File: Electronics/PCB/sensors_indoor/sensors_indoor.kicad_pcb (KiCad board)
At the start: 4 copper layers, 50 x 50 mm, 21 parts, among them J1 USB4125-GF-A, J2 Conn_ST_STDC14, J3 B5B-ZR, U1 STM32WBA5MMG, U10 MIC5219-3.3YM5, U2 SHT45-AD1F, U3 SCD41-D-R2, U4 SGP41, U5 LPS22DF, U6 TSOP38436, U7 FM24CL16B, U8 SPS30, U9 OPT4001DTSR

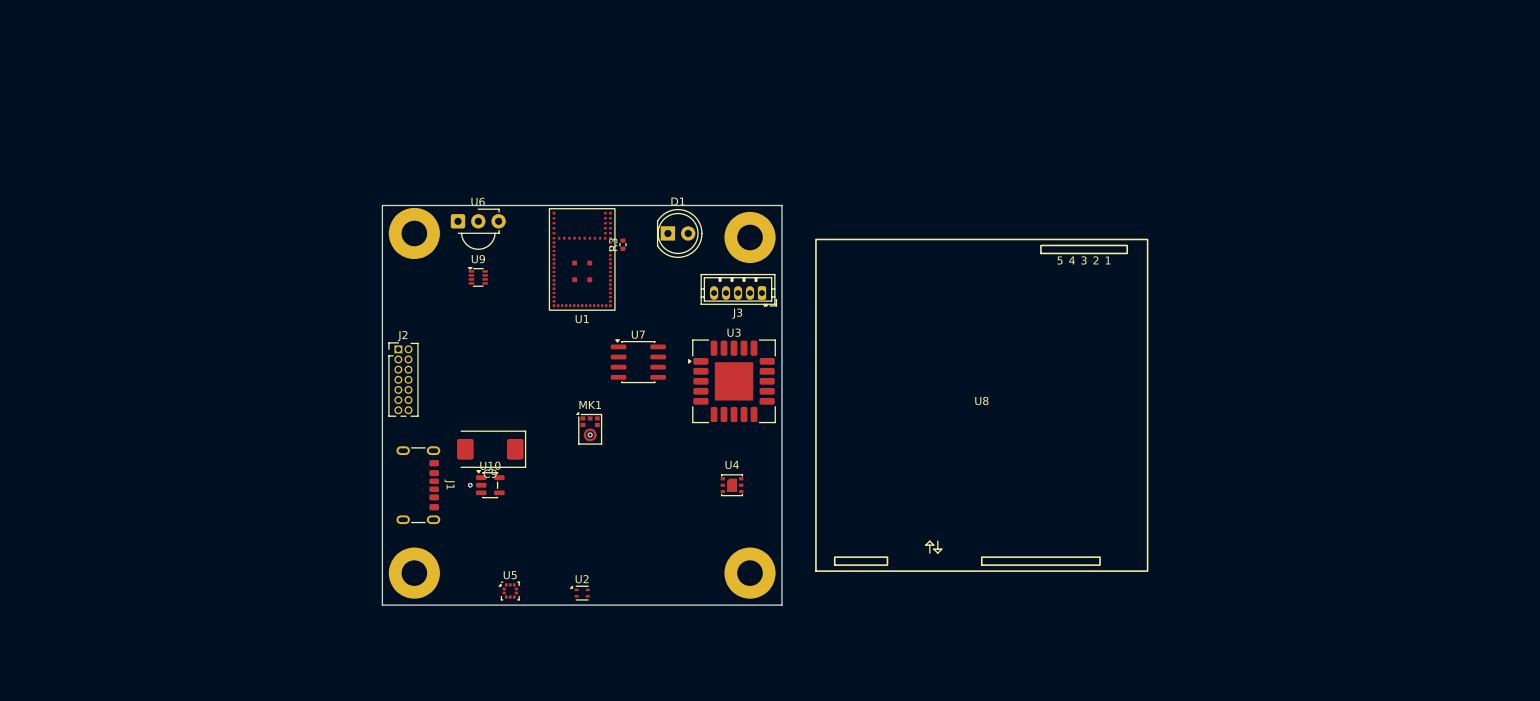
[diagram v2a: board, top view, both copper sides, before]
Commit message: Added mounting holes and power supply
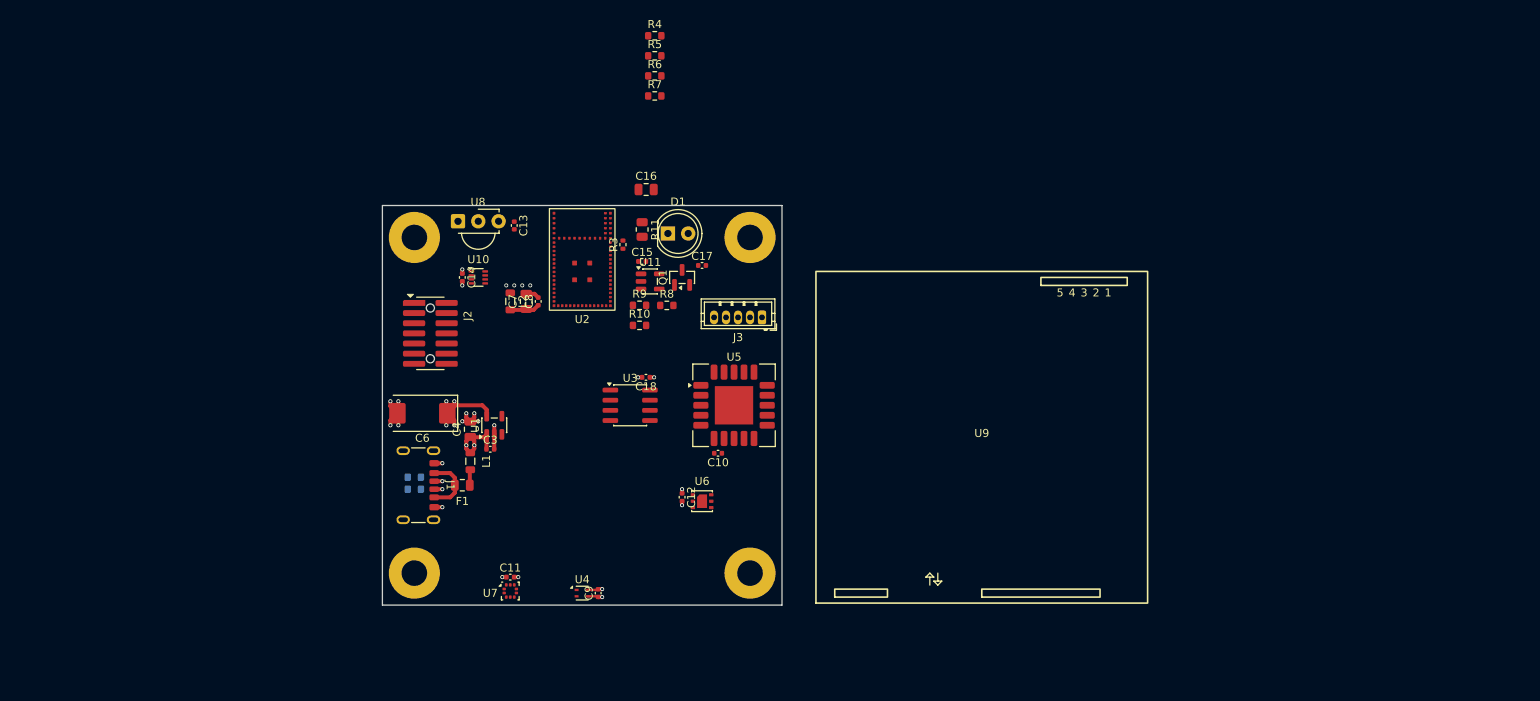
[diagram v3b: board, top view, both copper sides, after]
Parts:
- removed MK1: ICS-43434, Sensor_Audio:InvenSense_ICS-43434-6_3.5x2.65mm
- removed REF** (x4): MountingHole_3.2mm_M3_Pad, MountingHole:MountingHole_3.2mm_M3_Pad
- added C10: 0.1u, Capacitor_SMD:C_0402_1005Metric, F.Cu at (117.0, 106.0)
- added C11: 0.1u, Capacitor_SMD:C_0402_1005Metric, F.Cu at (91.0, 121.5)
- added C12: 0.1u, Capacitor_SMD:C_0402_1005Metric, F.Cu at (112.5, 111.5)
- added C13: 0.1u, Capacitor_SMD:C_0402_1005Metric, F.Cu at (91.5, 77.5)
- added C14: 0.1u, Capacitor_SMD:C_0402_1005Metric, F.Cu at (85.0, 84.0)
- added C15: 0.1u, Capacitor_SMD:C_0402_1005Metric, F.Cu at (107.5, 82.0)
- added C16: 4.7u, Capacitor_SMD:C_0805_2012Metric, F.Cu at (108.0, 73.0)
- added C17: 0.1u, Capacitor_SMD:C_0402_1005Metric, F.Cu at (115.0, 82.5)
- added C18: 0.1u, Capacitor_SMD:C_0402_1005Metric, F.Cu at (108.0, 96.5)
- added C3: 0.1u, Capacitor_SMD:C_0402_1005Metric, F.Cu at (88.5, 105.5)
- added C4: 4.7u, Capacitor_SMD:C_0805_2012Metric, F.Cu at (86.0, 103.0)
- added C7: 4.7u, Capacitor_SMD:C_0805_2012Metric, F.Cu at (93.0, 87.0)
- added C8: 0.1u, Capacitor_SMD:C_0402_1005Metric, F.Cu at (94.5, 87.0)
- added C9: 0.1u, Capacitor_SMD:C_0402_1005Metric, F.Cu at (102.0, 123.5)
- added F1: Polyfuse, Fuse:Fuse_0805_2012Metric, F.Cu at (85.0, 110.0)
- added H1: M3, MountingHole:MountingHole_3.2mm_M3_Pad, F.Cu at (79.0, 79.0)
- added H2: M3, MountingHole:MountingHole_3.2mm_M3_Pad, F.Cu at (121.0, 79.0)
- added H3: M3, MountingHole:MountingHole_3.2mm_M3_Pad, F.Cu at (79.0, 121.0)
- added H4: M3, MountingHole:MountingHole_3.2mm_M3_Pad, F.Cu at (121.0, 121.0)
- added L1: L_Ferrite, Inductor_SMD:L_0805_2012Metric, F.Cu at (86.0, 107.0)
- added L2: L_Ferrite, Inductor_SMD:L_0805_2012Metric, F.Cu at (91.0, 87.0)
- added Q1: DMN62D0U, Package_TO_SOT_SMD:SOT-23, F.Cu at (112.5, 84.0)
- added R1: 5.1k, Resistor_SMD:R_0603_1608Metric, B.Cu at (79.0, 110.5)
- added R10: 10k, Resistor_SMD:R_0603_1608Metric, F.Cu at (107.2, 90.0)
- added R11: 43R, Resistor_SMD:R_0805_2012Metric, F.Cu at (107.5, 78.0)
- added R2: 5.1k, Resistor_SMD:R_0603_1608Metric, B.Cu at (79.0, 109.0)
- added R4: X, Resistor_SMD:R_0603_1608Metric, F.Cu at (109.1, 53.8)
- added R5: X, Resistor_SMD:R_0603_1608Metric, F.Cu at (109.1, 56.3)
- added R6: X, Resistor_SMD:R_0603_1608Metric, F.Cu at (109.1, 58.8)
- added R7: X, Resistor_SMD:R_0603_1608Metric, F.Cu at (109.1, 61.3)
- added R8: 100R, Resistor_SMD:R_0603_1608Metric, F.Cu at (110.6, 87.5)
- added R9: 10k, Resistor_SMD:R_0603_1608Metric, F.Cu at (107.2, 87.5)
- added U11: 74LVC1G08, Package_TO_SOT_SMD:SOT-23-5, F.Cu at (108.5, 84.5)
- J2: value Conn_ST_STDC14 -> STDC14; footprint Connector_PinHeader_1.27mm:PinHeader_2x07_P1.27mm_Vertical -> ZMPlib:SAMTEC_FTSH-107-01-L-DV-K-A
- moved C6 9.62 mm to (80.0, 101.0)
- moved U1 7.52 mm to (89.0, 102.5), turned to 90 degrees
- moved U3 5.50 mm to (106.0, 100.0)
- moved J2 4.47 mm to (81.0, 91.0), turned to -90 degrees
- moved U6 4.25 mm to (115.0, 112.0)
- moved U9 4.00 mm to (150.0, 104.0)
- moved J3 3.05 mm to (122.5, 89.0)
- moved U5 3.00 mm to (119.0, 100.0)
- renumbered C9 to C6, U10 to U1, U9 to U10, U1 to U2, U7 to U3, U2 to U4, U3 to U5, U4 to U6, U5 to U7, U6 to U8, U8 to U9
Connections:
- D1 pad 1: unconnected-(D1-K-Pad1) -> Net-(D1-K)
- D1 pad 2: unconnected-(D1-A-Pad2) -> Net-(D1-A)
- J3 pad 2: unconnected-(J3-Pin_2-Pad2) -> UART_MOSI
- J3 pad 3: unconnected-(J3-Pin_3-Pad3) -> UART_MISO
- U10 pad 1: unconnected-(U9-VDD-Pad1) -> +3.3V
- U10 pad 5: unconnected-(U9-SCL-Pad5) -> I2C3_SCL
- U10 pad 8: unconnected-(U9-SDA-Pad8) -> I2C3_SDA
- U2 pad 13: unconnected-(U1-PA8-Pad13) -> UART_MISO
- U2 pad 2: GND -> unconnected-(U2-GND-Pad2)
- U2 pad 3: GND -> unconnected-(U2-GND-Pad3)
- U2 pad 30: /indoor_MCU/I2S_SCK -> unconnected-(U2-PB6-Pad30)
- U2 pad 31: /indoor_MCU/I2S_SD -> unconnected-(U2-PB7-Pad31)
- U2 pad 33: /indoor_MCU/I2S_FS -> unconnected-(U2-PB5-Pad33)
- U2 pad 4: GND -> unconnected-(U2-GND-Pad4)
- U2 pad 5: GND -> unconnected-(U2-GND-Pad5)
- U2 pad 56: GND -> unconnected-(U2-GND-Pad56)
- U2 pad 59: GND -> unconnected-(U2-GND-Pad59)
- U2 pad 9: unconnected-(U1-PB14-Pad9) -> UART_MOSI
- U3 pad 8: unconnected-(U7-VDD-Pad8) -> +3.3V
- U4 pad 1: I2C1_SDA -> I2C3_SDA
- U4 pad 2: I2C1_SCL -> I2C3_SCL
- U4 pad 3: Net-(U2-VDD) -> +3.3V
- U5 pad 10: unconnected-(U3-SDA-Pad10) -> I2C1_SDA
- U5 pad 19: Net-(U3-VDD-Pad19) -> +3.3V
- U5 pad 7: Net-(U3-VDD-Pad19) -> +3.3V
- U5 pad 9: unconnected-(U3-SCL-Pad9) -> I2C1_SCL
- U6 pad 1: unconnected-(U4-VDD-Pad1) -> Net-(U6-VDD)
- U6 pad 3: unconnected-(U4-SDA-Pad3) -> I2C1_SDA
- U6 pad 6: unconnected-(U4-SCL-Pad6) -> I2C1_SCL
- U7 pad 10: unconnected-(U5-VDD-Pad10) -> +3.3V
- U8 pad 3: unconnected-(U6-Vs-Pad3) -> +3.3V
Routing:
- net GND: track 0.00 -> 22.0 mm, vias 0 -> 18
- net +3.3V: track 0.00 -> 16.6 mm, vias 0 -> 10
- net +5V: track 0.00 -> 8.92 mm, vias 0 -> 2
- net /VBUS: track 0.00 -> 7.52 mm
- net /indoor_MCU/VDD_MCU: track 0.00 -> 3.74 mm
- net Net-(F1-Pad2): track 0.00 -> 1.96 mm
- net Net-(J1-CC2): track 0.00 -> 1.02 mm, vias 0 -> 1
- net Net-(J1-CC1): track 0.00 -> 1.02 mm, vias 0 -> 1
- net Net-(U6-VDD): track 0.00 -> 0.52 mm, vias 0 -> 1
- net (no net): vias 1 -> 0
- added copper zone on In2.Cu, net +3.3V

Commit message: Swapped sides of everything and started routing
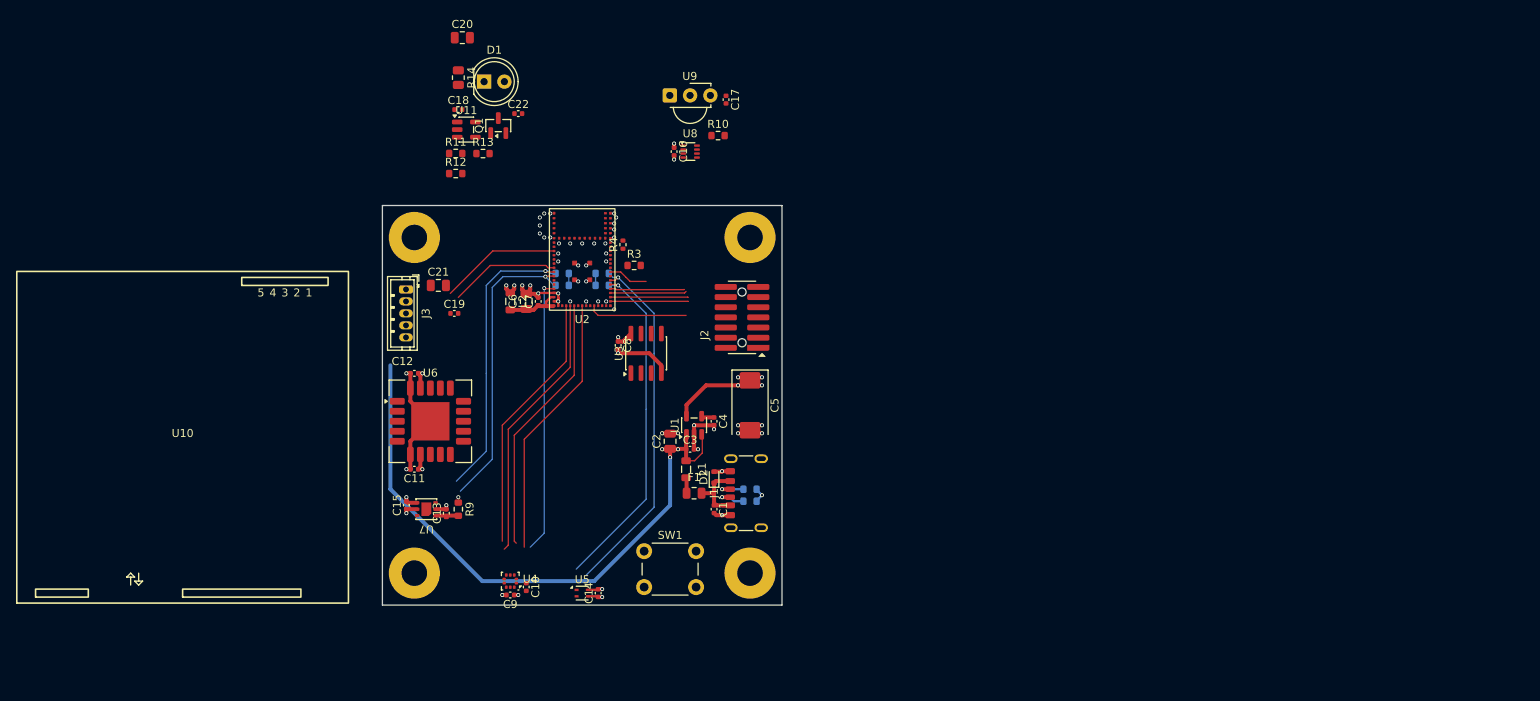
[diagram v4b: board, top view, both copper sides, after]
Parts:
- added C1: 10n, Capacitor_SMD:C_0402_1005Metric, F.Cu at (116.5, 113.0)
- added C10: 0.1u, Capacitor_SMD:C_0402_1005Metric, F.Cu at (93.0, 122.7)
- added C12: 0.1u, Capacitor_SMD:C_0402_1005Metric, F.Cu at (79.0, 96.0)
- added C15: 1u, Capacitor_SMD:C_0402_1005Metric, F.Cu at (78.0, 112.5)
- added C19: 0.1u, Capacitor_SMD:C_0402_1005Metric, F.Cu at (84.0, 88.5)
- added C21: 4.7u, Capacitor_SMD:C_0805_2012Metric, F.Cu at (82.0, 85.0)
- added C4: 470p, Capacitor_SMD:C_0402_1005Metric, F.Cu at (116.5, 102.0)
- added D2: ESD5Z5.0, Diode_SMD:D_SOD-523, F.Cu at (116.5, 109.0)
- added R10: 10k, Resistor_SMD:R_0603_1608Metric, F.Cu at (117.0, 66.2)
- added R3: 10k, Resistor_SMD:R_0603_1608Metric, F.Cu at (106.5, 82.5)
- added R9: 4.7R, Resistor_SMD:R_0603_1608Metric, F.Cu at (84.5, 113.0)
- added SW1: SW_Push, Button_Switch_THT:SW_PUSH_6mm, F.Cu at (107.8, 118.2)
- C13: renamed from C12; value 0.1u -> 1u
- F1: value Polyfuse -> 500mA
- L1, L2: value L_Ferrite -> 600R
- R5: renamed from R4; value X -> 4.7k; moved to B.Cu
- R6: renamed from R5; value X -> 1.5k; moved to B.Cu
- R7: renamed from R6; value X -> 4.7k; moved to B.Cu
- R8: renamed from R7; value X -> 1.5k; moved to B.Cu
- moved U10 100.0 mm to (50.0, 104.0)
- moved J3 44.7 mm to (78.0, 85.5), turned to -90 degrees
- moved J1 43.2 mm to (121.6, 111.0), turned to 90 degrees
- moved R2 42.1 mm to (121.0, 112.0), turned to 0 degrees
- moved R1 42.0 mm to (121.0, 110.5), turned to 0 degrees
- moved C5 41.0 mm to (121.0, 100.0), turned to -90 degrees
- moved J2 39.1 mm to (120.0, 89.0), turned to 90 degrees
- moved C11 38.1 mm to (79.0, 108.0)
- moved U6 38.1 mm to (81.0, 102.0)
- moved U7 34.5 mm to (80.5, 113.0), turned to 180 degrees
- moved R6 31.0 mm to (97.5, 85.0), turned to 180 degrees
- moved C16 30.8 mm to (111.5, 68.2)
- moved C17 30.8 mm to (118.0, 61.8)
- moved U8 30.8 mm to (113.5, 68.2)
- moved U9 30.8 mm to (111.0, 61.2)
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- renumbered C10 to C11, C9 to C14, C14 to C16, C13 to C17, C15 to C18, C4 to C2, C16 to C20, C17 to C22, C6 to C5, C7 to C6, C8 to C7, C18 to C8, C11 to C9, R9 to R11, R10 to R12, R8 to R13, R11 to R14, R3 to R4, U9 to U10, U7 to U4, U4 to U5, U5 to U6, U6 to U7, U10 to U8, U8 to U9
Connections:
- J3 pad 1: unconnected-(J3-Pin_1-Pad1) -> +5V
- U2 pad 11: unconnected-(U2-PB12-Pad11) -> IR_OUT
- U2 pad 18: /indoor_MCU/SPI_SCLK -> SPI_SCLK
- U2 pad 25: unconnected-(U2-PA2-Pad25) -> INT_PRES
- U2 pad 26: /indoor_MCU/SPI_MISO -> SPI_MISO
- U2 pad 27: /indoor_MCU/SPI_CS -> SPI_CS
- U2 pad 29: /indoor_MCU/SPI_MOSI -> SPI_MOSI
- U2 pad 35: unconnected-(U2-PB4-Pad35) -> IR_IN
- U2 pad 44: unconnected-(U2-PB15-Pad44) -> INT_ALS
- U2 pad 8: unconnected-(U2-PA9-Pad8) -> IR_CARRIER
- U4 pad 1: unconnected-(U7-Vdd_IO-Pad1) -> +3.3V
- U4 pad 2: /indoor_sensors/SPI_SCLK -> SPI_SCLK
- U4 pad 4: /indoor_sensors/SPI_MOSI -> SPI_MOSI
- U4 pad 5: /indoor_sensors/SPI_MISO -> SPI_MISO
- U4 pad 6: /indoor_sensors/SPI_CS -> SPI_CS
- U5 pad 1: I2C3_SDA -> I2C1_SDA
- U5 pad 2: I2C3_SCL -> I2C1_SCL
- U6 pad 10: I2C1_SDA -> I2C3_SDA
- U6 pad 9: I2C1_SCL -> I2C3_SCL
- U7 pad 3: I2C1_SDA -> I2C3_SDA
- U7 pad 4: unconnected-(U6-N/A-Pad4) -> GND
- U7 pad 5: unconnected-(U6-VDDH-Pad5) -> +3.3V
- U7 pad 6: I2C1_SCL -> I2C3_SCL
- U8 pad 2: unconnected-(U10-ADDR-Pad2) -> +3.3V
- U8 pad 5: I2C3_SCL -> I2C1_SCL
- U8 pad 8: I2C3_SDA -> I2C1_SDA
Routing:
- net +5V: track 8.92 -> 78.4 mm, vias 2 -> 3
- net I2C1_SDA: track 0.00 -> 45.1 mm, vias 0 -> 1
- net I2C1_SCL: track 0.00 -> 42.8 mm, vias 0 -> 1
- net GND: track 22.0 -> 59.7 mm, vias 18 -> 55
- net I2C3_SCL: track 0.00 -> 37.2 mm, vias 0 -> 1
- net I2C3_SDA: track 0.00 -> 36.7 mm, vias 0 -> 1
- net SPI_SCLK: track 0.00 -> 34.4 mm, vias 0 -> 1
- net SPI_MISO: track 0.00 -> 33.9 mm
- net SPI_MOSI: track 0.00 -> 33.2 mm
- net SPI_CS: track 0.00 -> 32.9 mm
- net INT_PRES: track 0.00 -> 32.8 mm
- net +3.3V: track 16.6 -> 32.4 mm, vias 10 -> 14
- net UART_MOSI: track 0.00 -> 15.2 mm
- net UART_MISO: track 0.00 -> 13.8 mm
- net /indoor_MCU/SWO: track 0.00 -> 12.4 mm
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
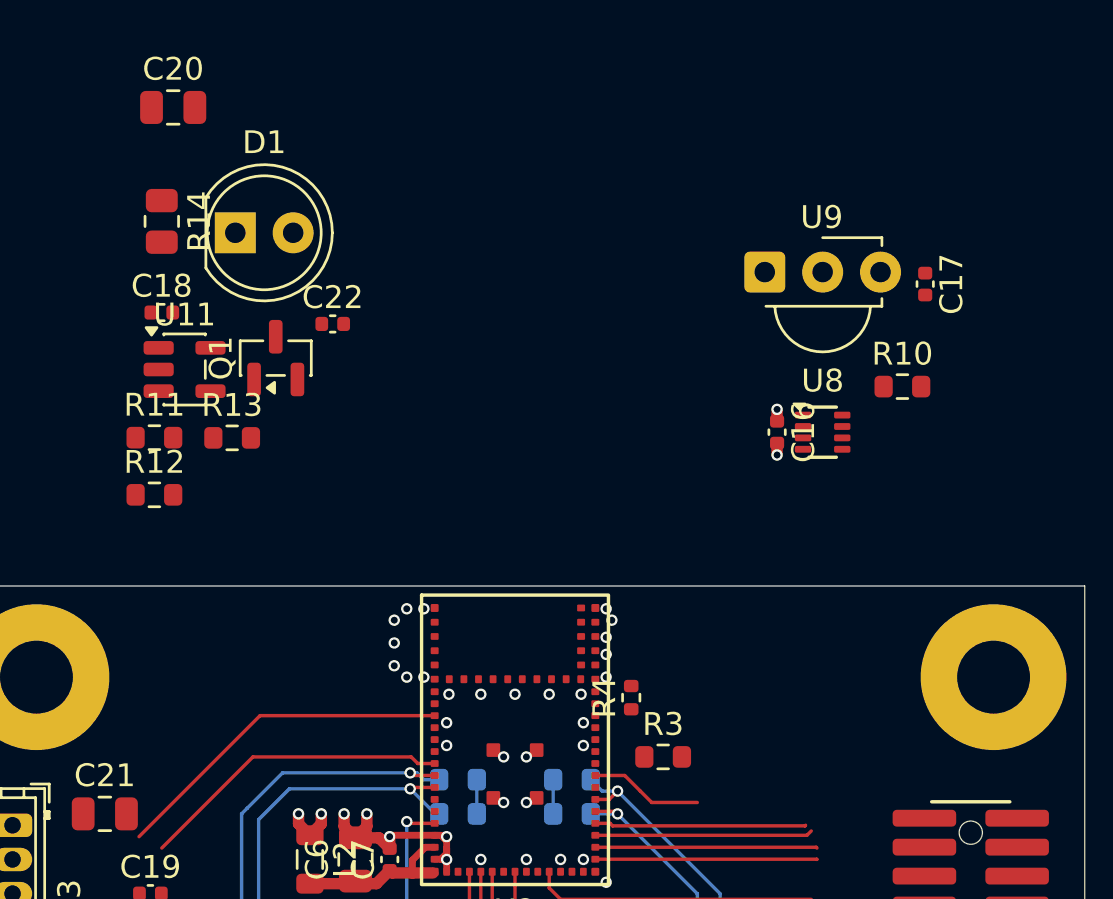
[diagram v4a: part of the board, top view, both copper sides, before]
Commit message: Updated PCB with SMD IR tx/rx
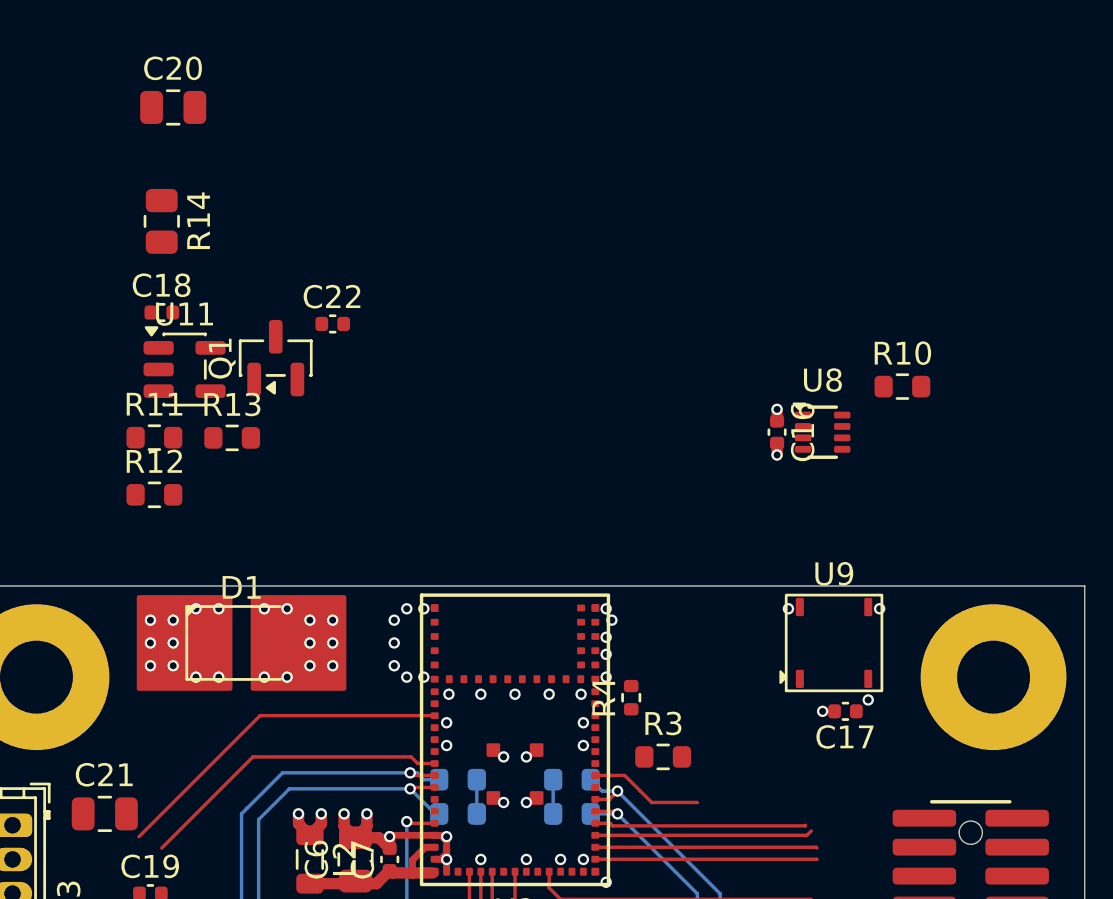
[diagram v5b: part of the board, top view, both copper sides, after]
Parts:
- D1: footprint LED_THT:LED_D5.0mm_Clear -> DWlib:Osram_LED_SFH-4243
- U9: footprint OptoDevice:Vishay_MINICAST-3Pin -> DWlib:Vishay_BELOBOG-4Pin
- moved C17 19.1 mm to (114.5, 80.5), turned to 180 degrees
- moved D1 18.0 mm to (88.0, 77.5)
- moved U9 16.6 mm to (114.0, 77.5)
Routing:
- net GND: vias 55 -> 58
- net +3.3V: vias 14 -> 15
- net (no net): vias 0 -> 20
